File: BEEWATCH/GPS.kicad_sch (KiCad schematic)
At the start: 6 parts, among them Q1 Si1442DH, U3 L80-R

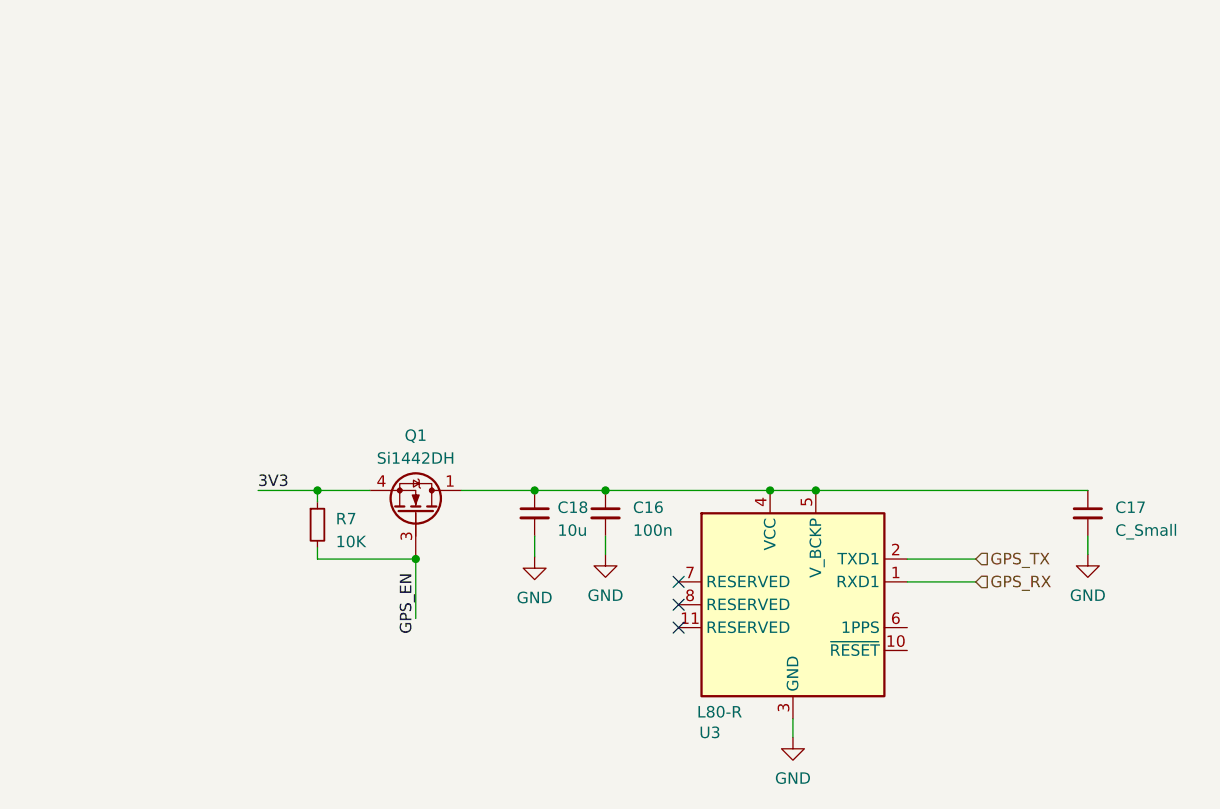
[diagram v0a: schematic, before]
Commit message: Inverted F Antenna designed
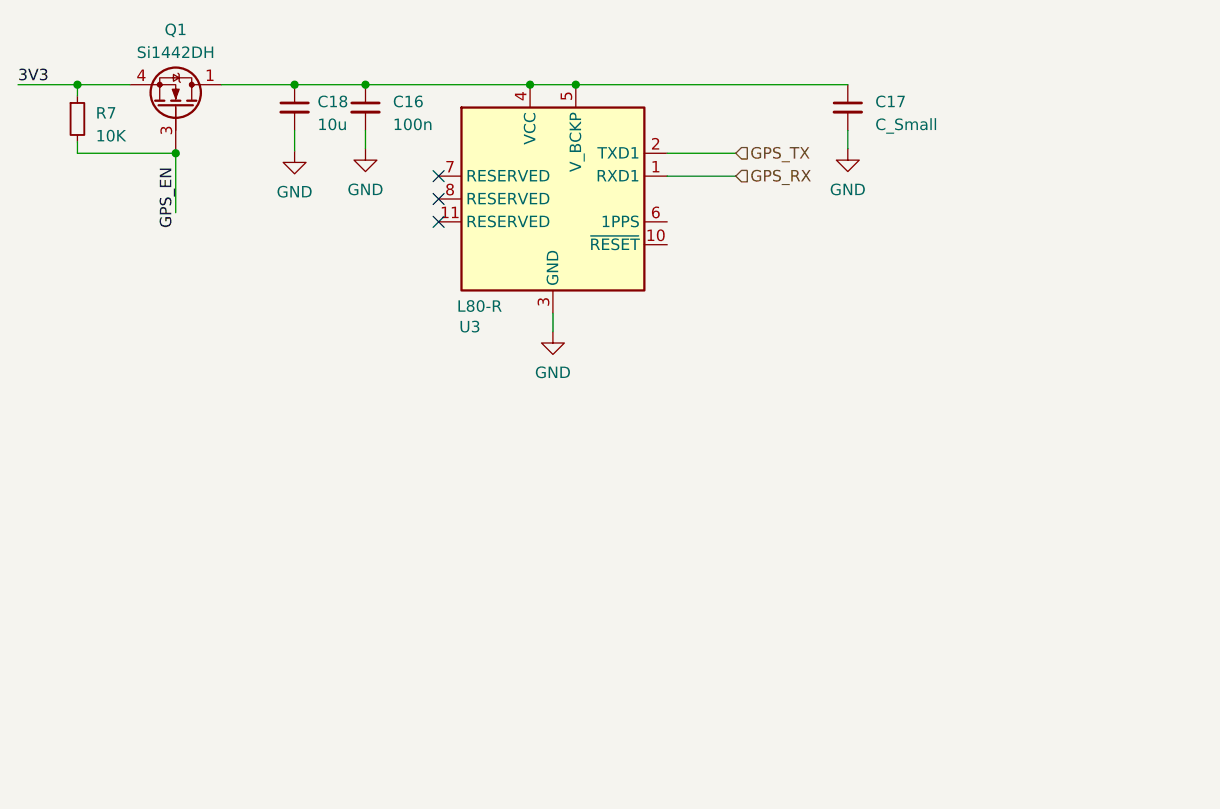
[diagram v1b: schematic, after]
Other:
- moved on the sheet: C16, C17, C18, Q1, R7, U3
